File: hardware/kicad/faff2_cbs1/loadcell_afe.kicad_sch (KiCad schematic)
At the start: 52 parts, among them J501 1729076, J502 8510-4500PL, U501 ADS1235

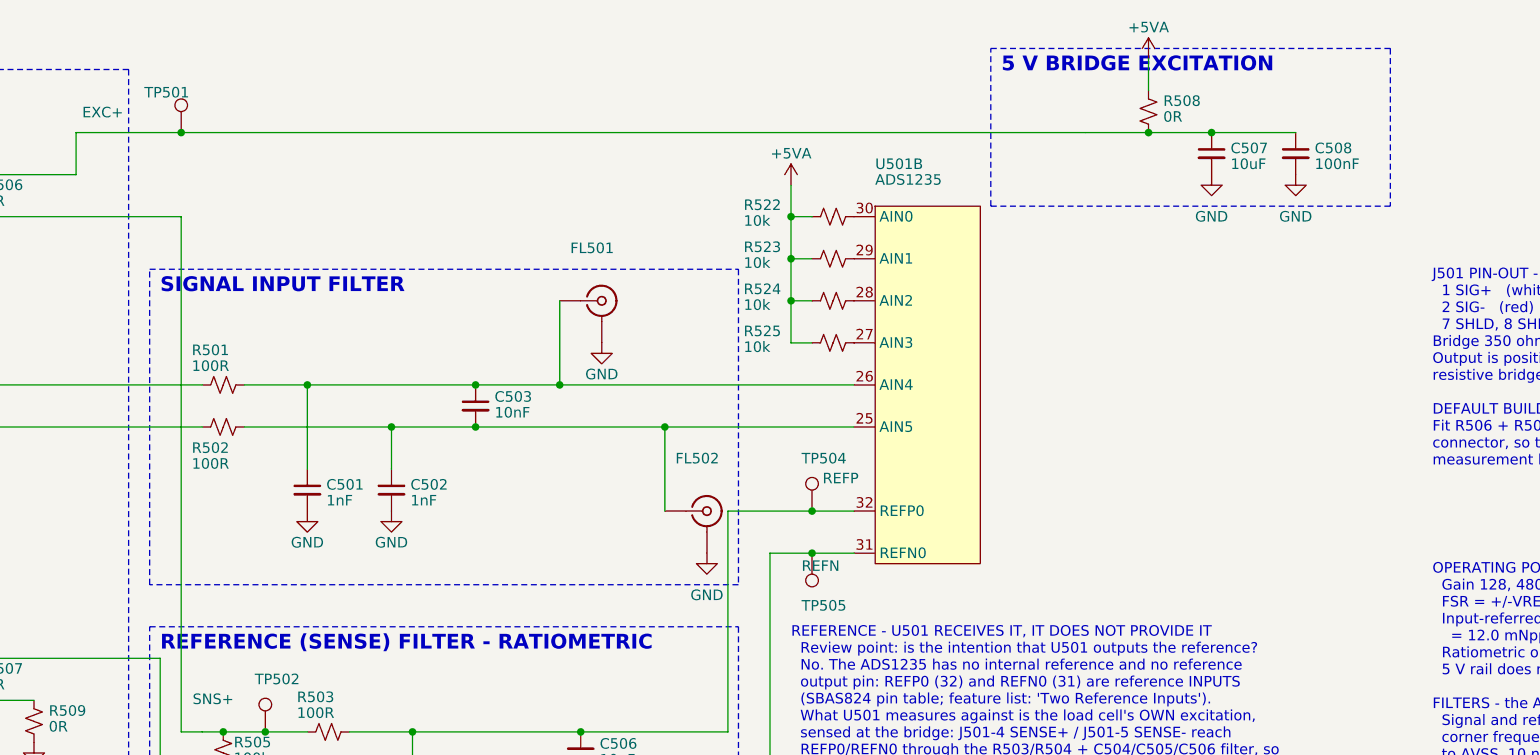
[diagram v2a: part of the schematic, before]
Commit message: review r2 item 8: one placement rule for every power symbol's net name
"Directly above it, centre justified, and close" - applied as no sideways
offset, centred, 3.81 mm away: above a rail arrow, below a ground. All 283
power symbols now carry it; 103 did not, most left-anchored rather than centred
and a few offset up to 7.6 mm sideways by round 1's auto-placer.

The ground mirror is an interpretation and is flagged as such: "above" a GND
symbol is where its wire arrives, and 137 instances plus every convention put
GND's name under the triangle. One line to change if the captain meant it
literally.

What makes this different from round 1 is that the label is now PINNED, so
everything else moves instead - the symbol along its own stub, a note to the
nearest clear spot, a block box outward (five rectangles grew where a name sat
on a border with clear space beyond), and two PWR_FLAGs placed by hand because
their 9.5 mm names do not fit the 10 mm rail runs they tap.

Thirteen of 283 still graze a wire, body or note on the two densest sheets and
are listed in the decisions file rather than hidden. Each needs the parts around
it respaced, which is more than a label sweep should do unasked - the TIM1 note
on motor_drive in particular has nowhere to go: no clear position exists for a
47.6 x 8.7 mm box anywhere in that block.

Also recorded: my own severity metric scored wire-through-text at zero for a
while, because a wire is a zero-thickness segment and box-intersection depth
against it is always 0. For those, severity is how far inside the box the line
sits. A render caught it; the number did not.

ERC 0 errors / 0 warnings at severity-all; 412 components, 259 nets, node sets
identical to before the batch. Review PDF regenerated once, here, for the whole
of round 2.

Co-Authored-By: Claude Opus 5 <noreply@anthropic.com>
Claude-Session: https://claude.ai/code/session_01PFWfwT8RZc8Zqn8vgZxV8j
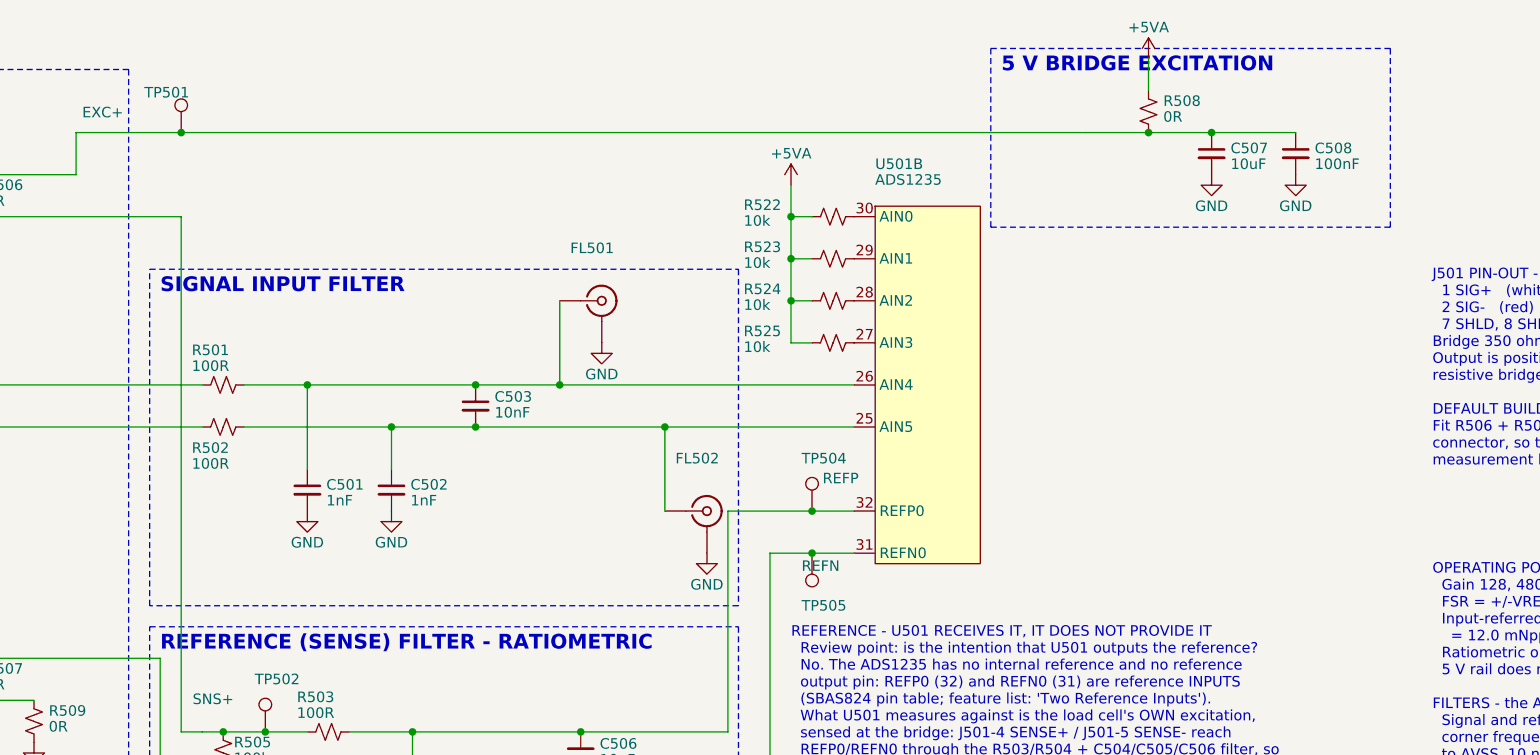
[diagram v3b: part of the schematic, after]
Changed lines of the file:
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@@
 		)
 		(property "Value" "GND"
-			(at 162.56 80.01 0)
+			(at 162.56 78.74 0)
 			(do_not_autoplace yes)
 			(effects
@@
 		)
 		(property "Value" "GND"
-			(at 223.52 34.29 0)
+			(at 223.52 33.02 0)
 			(do_not_autoplace yes)
 			(effects
@@
 		)
 		(property "Value" "GND"
-			(at 233.68 34.29 0)
+			(at 233.68 33.02 0)
 			(do_not_autoplace yes)
 			(effects
@@
 	(rectangle
 		(start 95.25 40.64)
-		(end 166.37 78.74)
+		(end 166.37 81.28)
 		(stroke
 			(width 0.1524)
@@
 	(rectangle
 		(start 196.85 13.97)
-		(end 245.11 33.02)
+		(end 245.11 35.56)
 		(stroke
 			(width 0.1524)
